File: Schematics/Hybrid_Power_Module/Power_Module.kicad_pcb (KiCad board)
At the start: 4 copper layers, 69.5 x 60 mm, 133 parts, among them J1 ScrewSwitch, J2 Battery, J3 ScrewSwitch, J4 GSE, J5 USB_C_Female_USB2_Small, J6 SWD_B, J7 Stack Male Edge Connector, Q1 AO4447A, Q2 SI2305CDS, Q3 DMN6040SSD-13, SW1 SW_STM_RESET, SW2 SW_STM_BOOT_MODE, U1 TPS61175PWPR, U10 LM66100DCKR, U11 LM66100DCKR, U12 AMS1117-3.3, U13 CP2102N-A02-GQFN20R, U14 STM32F103CBT6, U15 TCAN1051HGVDR, U16 BY25Q128ES, U2 LM74700QDBVRQ1, U3 LM74700QDBVRQ1, U4 ACS37041KLHBLT-010B3, U5 ACS37041KLHBLT-010B5, U6 INA187A, U7 LMR51430XDDCR, U8 LMR51430XDDCR, U9 LM66100DCKR, Y1 X322516MMB4SI

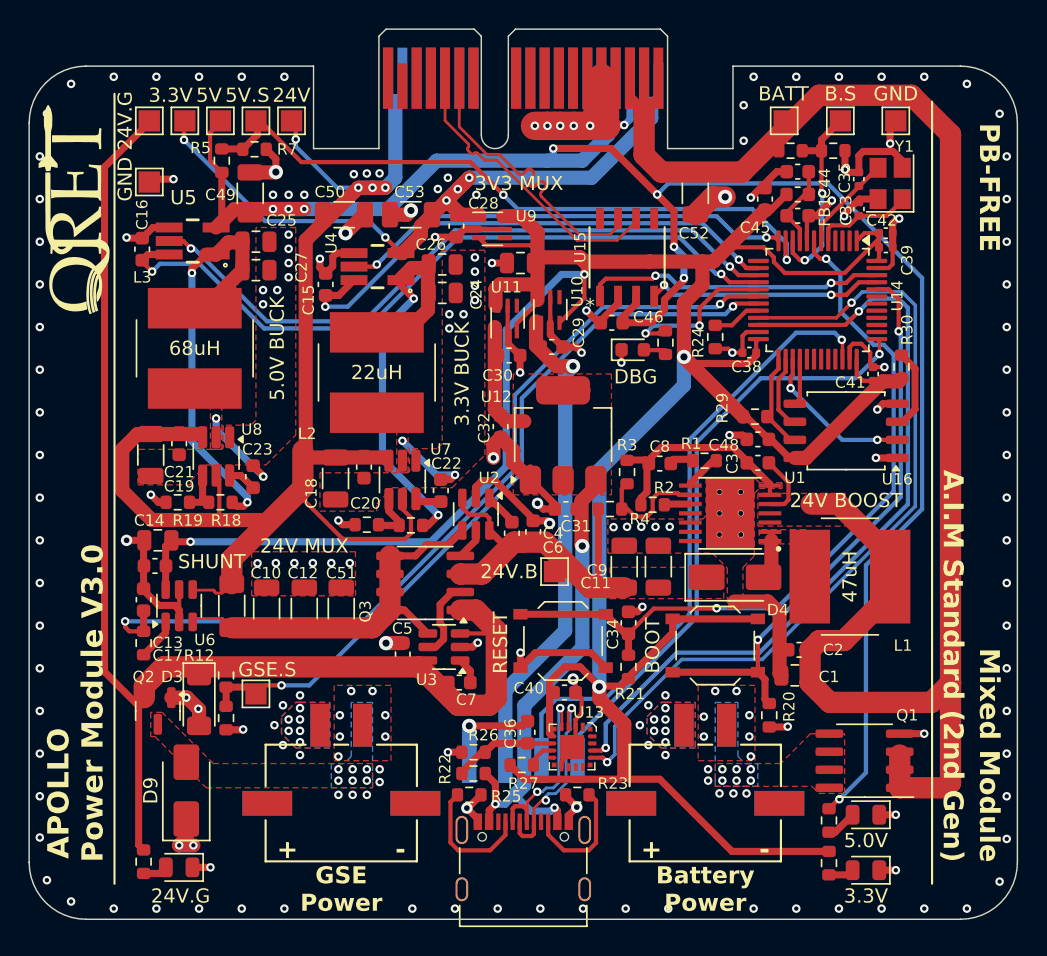
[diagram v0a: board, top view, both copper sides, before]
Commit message: fix: Updates after testing, for next revision
 - add current limiting to GSE RPP zener shunt
 - switched 5v current sensor
 - flipped CAN and UART polarity
 - add 3.3v reference to CAN transceiver
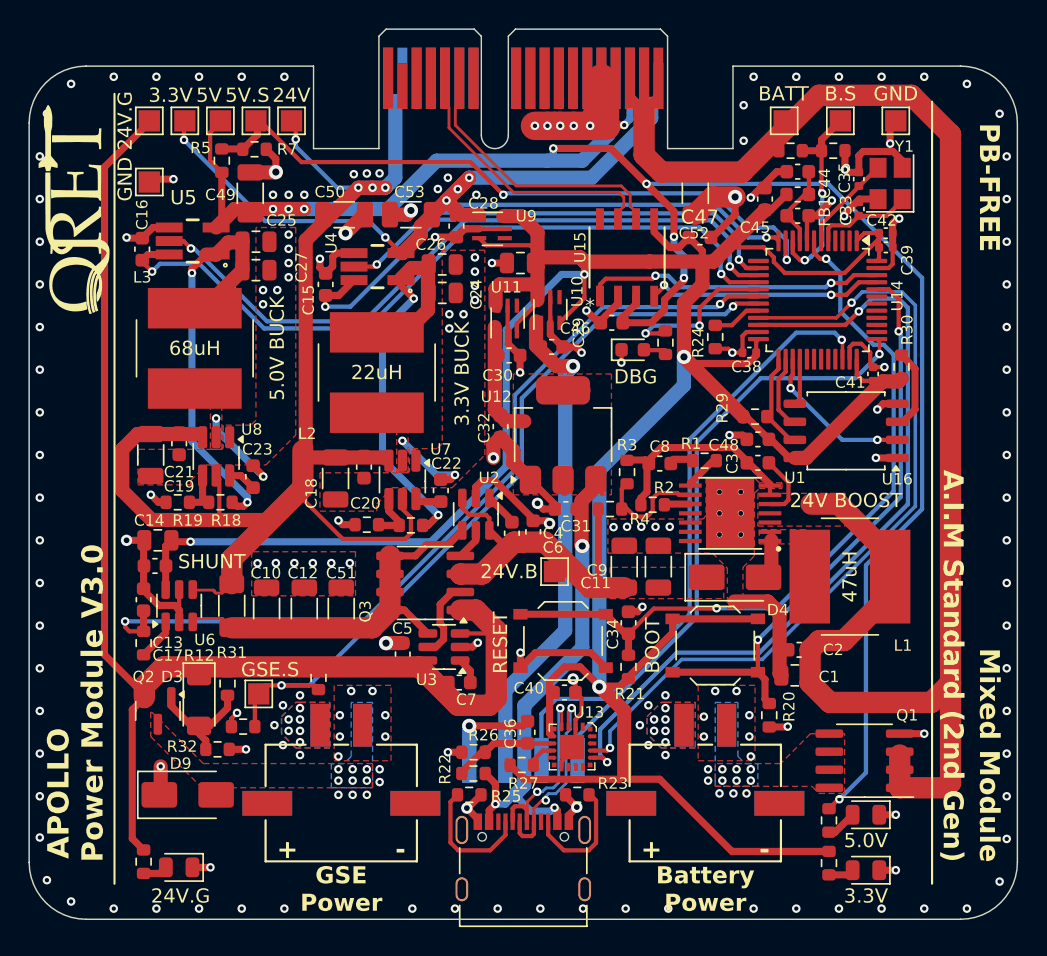
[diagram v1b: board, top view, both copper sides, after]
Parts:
- added C47: 100nF, Capacitor_SMD:C_0603_1608Metric, F.Cu at (177.4, 51.8)
- added R31: 9.1k, Resistor_SMD:R_0603_1608Metric, F.Cu at (144.2, 83.2)
- added R32: 15k, Resistor_SMD:R_0603_1608Metric, F.Cu at (143.5, 87.8)
- U5: value ACS37041KLHBLT-010B5 -> ACS37041KLHBLT-010B3
- moved R14 6.50 mm to (150.6, 82.8)
- moved R15 1.34 mm to (145.3, 86.2), turned to 0 degrees
- moved D9 0.32 mm to (141.4, 91.0), turned to 0 degrees
- moved TP9 0.20 mm to (146.4, 83.9)
- turned C46 to 180 degrees
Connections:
- C46 pad 1: GND -> 5V_PSU
- C46 pad 2: 5V_PSU -> GND
- D3 pad 2: GND -> Net-(D3-A)
- J7 pad B13: CAN_P -> CAN_N
- J7 pad B14: CAN_N -> CAN_P
- Q2 pad 1: GND -> Net-(D3-A)
- U13 pad 17: USART_TX -> USART_RX
- U13 pad 18: USART_RX -> USART_TX
- U15 pad 5: unconnected-(U15-NC-Pad5) -> 3.3V_MUX
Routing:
- net Net-(D3-A): track 0.00 -> 8.06 mm
- net 3.3V_MUX: track 222.7 -> 228.9 mm
- net CAN_N: track 21.0 -> 17.3 mm
- net CAN_P: track 21.0 -> 17.3 mm
- net GSE_SENSE: track 51.9 -> 53.7 mm
- net USART_TX: track 58.5 -> 56.8 mm
- net 5V_CURR_SENSE: track 47.7 -> 49.4 mm
- net 5V_ACS_PWR: track 51.8 -> 53.4 mm
- net USART_RX: track 55.7 -> 57.2 mm
- net 3.3V_ACS_PWR: track 38.3 -> 39.8 mm
- net 3.3V_CURR_SENSE: track 32.0 -> 32.7 mm
- net 24V_GSE: track 92.5 -> 92.0 mm
- net GND: track 210.3 -> 209.8 mm, vias 194 -> 192
